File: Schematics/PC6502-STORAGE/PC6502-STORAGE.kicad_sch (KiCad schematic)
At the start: 25 parts, among them J1 BUS, J2 Conn_02x26_Top_Bottom, J3 CLK_SLOW, J99 Conn_02x05_Odd_Even, U1 ATF1502AS

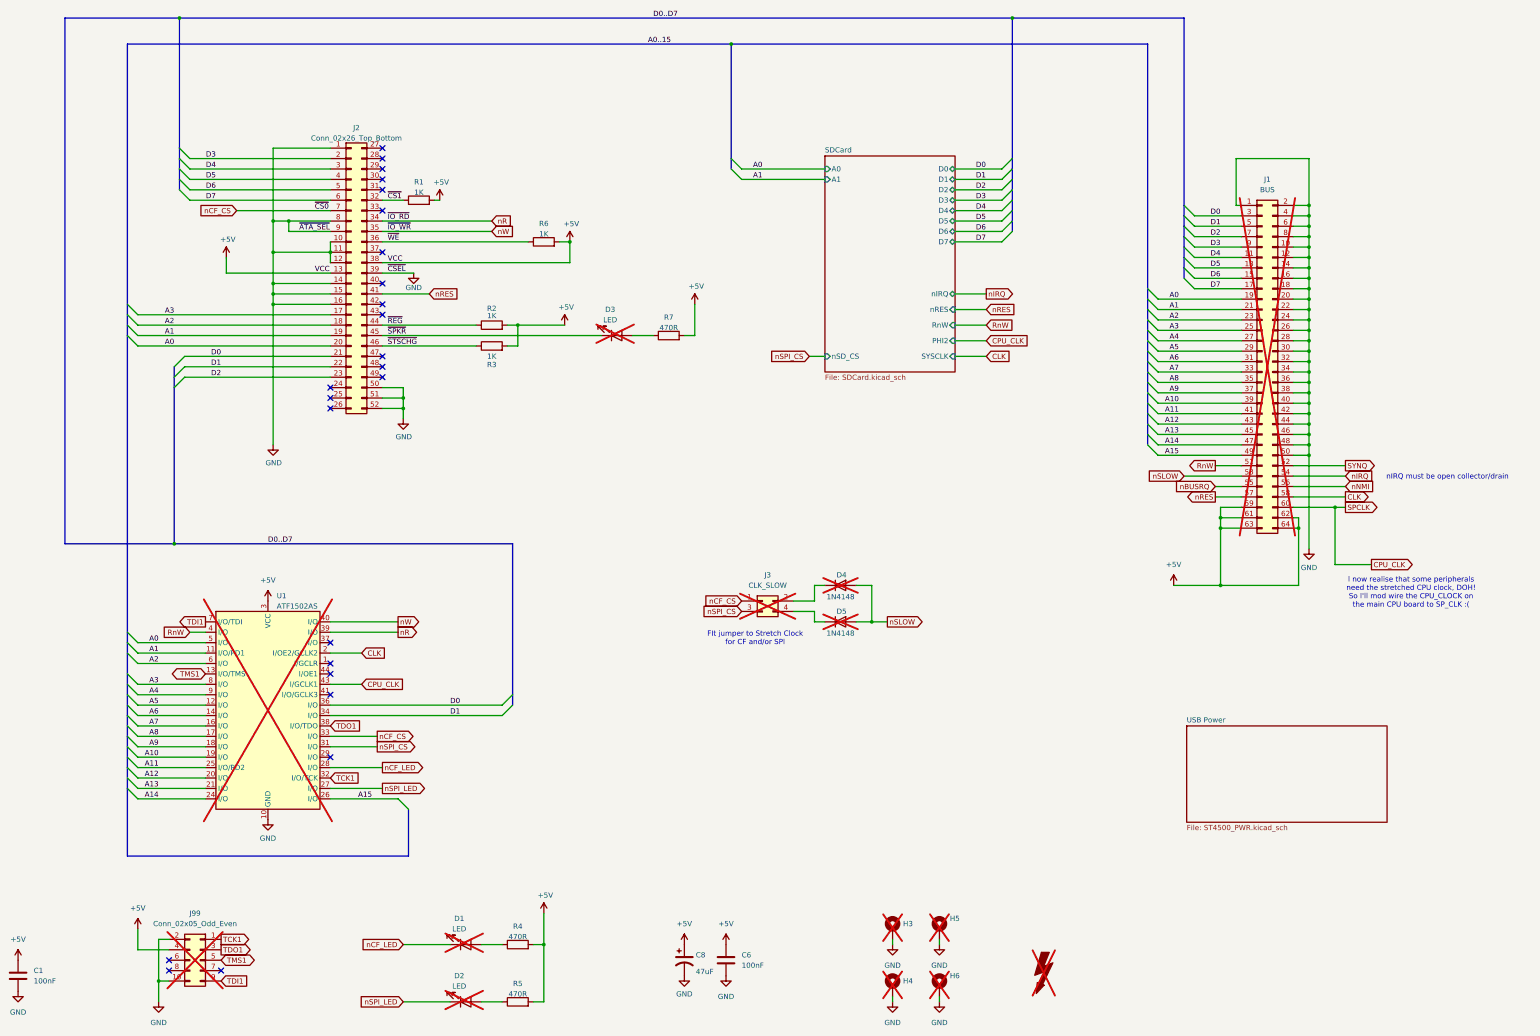
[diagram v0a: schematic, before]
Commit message: Tidy up and simplify
Created schematic for FM & Speech sound board
Made Storage board just for Compact Flash (CF) storage
Routed Storage PCB
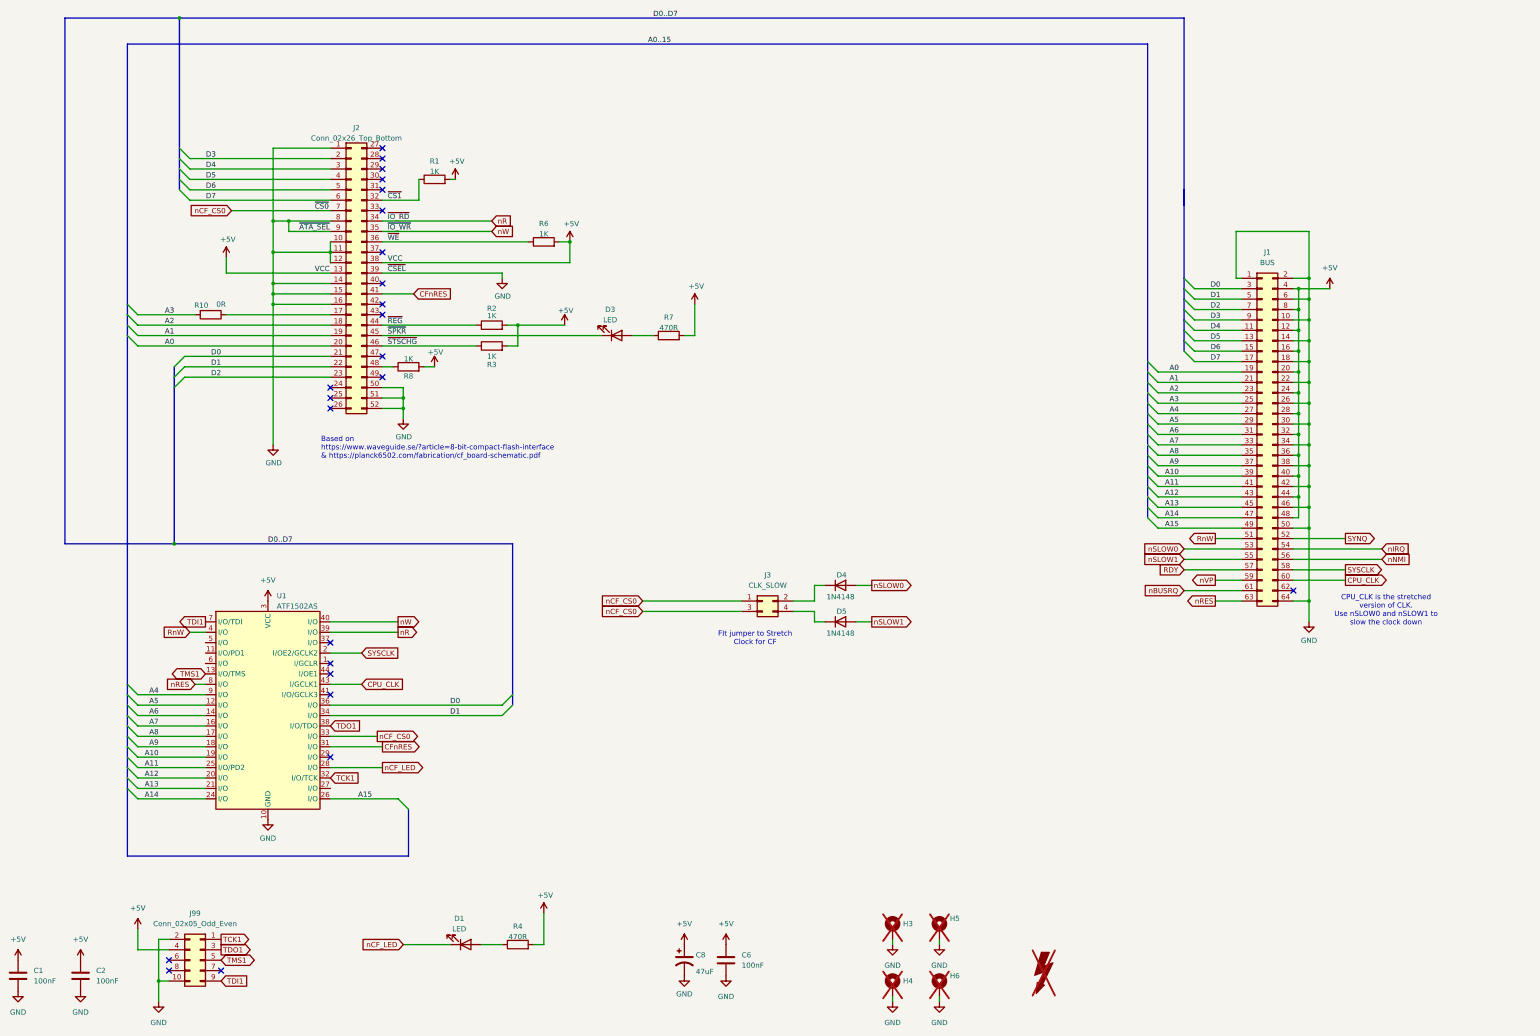
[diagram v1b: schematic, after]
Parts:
- removed D2: LED, LTL-4221NHBP:LTL4221NHBP, symbol Device:LED
- removed R5: 470R, Resistor_SMD:R_0603_1608Metric_Pad0.98x0.95mm_HandSolder, symbol Device:R
- added C2: 100nF, Capacitor_SMD:C_0805_2012Metric, symbol Device:C
- added R10: 0R, Resistor_SMD:R_0603_1608Metric_Pad0.98x0.95mm_HandSolder, symbol Device:R
- added R8: 1K, Resistor_SMD:R_0603_1608Metric_Pad0.98x0.95mm_HandSolder, symbol Device:R
- D1, D3, D4, D5, J1, J3, J99, U1: now fitted
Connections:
- net +5V: now also J1.12 (Pin_12), J1.16 (Pin_16), J1.20 (Pin_20), J1.24 (Pin_24), J1.28 (Pin_28), J1.32 (Pin_32), J1.36 (Pin_36), J1.4 (Pin_4), J1.40 (Pin_40), J1.44 (Pin_44), J1.48 (Pin_48), J1.8 (Pin_8), C2.1, R8.2; no longer J1.59 (Pin_59), J1.61 (Pin_61), J1.62 (Pin_62), J1.63 (Pin_63), J1.64 (Pin_64)
- net A0: no longer U1.5 (I/O)
- net A1: no longer U1.11 (I/O/PD1)
- net A2: no longer U1.6 (I/O)
- net A3: now also R10.2; no longer J2.17 (Pin_17), U1.8 (I/O)
- net GND: now also J1.64 (Pin_64), C2.2; no longer J1.12 (Pin_12), J1.16 (Pin_16), J1.20 (Pin_20), J1.24 (Pin_24), J1.28 (Pin_28), J1.32 (Pin_32), J1.36 (Pin_36), J1.4 (Pin_4), J1.40 (Pin_40), J1.44 (Pin_44), J1.48 (Pin_48), J1.8 (Pin_8)
- net nBUSRQ: now also J1.61 (Pin_61); no longer J1.55 (Pin_55)
- net nRES: now also J1.63 (Pin_63), U1.8 (I/O); no longer J1.57 (Pin_57), J2.41 (Pin_41)
- net at J2.48 (Pin_48): now also R8.1
- net CLK renamed SYSCLK
- net nCF_CS renamed nCF_CS0
- net nCF_CS0: now also J3.3 (Pin_3)
- net nSLOW renamed nSLOW0
- net nSLOW0: no longer D5.2 (A)
- net nSPI_CS renamed CFnRES
- net CFnRES: now also J2.41 (Pin_41); no longer J3.3 (Pin_3)
- net nSPI_LED: no longer names the net of U1.27 (I/O)
- new net: J2.17 (Pin_17), R10.1
- new net RDY: J1.57 (Pin_57)
- new net nSLOW1: D5.2 (A), J1.55 (Pin_55)
- new net nVP: J1.59 (Pin_59)
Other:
- removed sheet SDCard
- removed sheet USB Power
- note added: "Based on https://www.waveguide.se/?article=8-bit-compact-flash-interface & https://planck6502.com/fabrication/cf_board-schematic.pdf"
- note added: "CPU_CLK is the stretched version of CLK. Use nSLOW0 and nSLOW1 to slow the clock down"
- note added: "FIt jumper to Stretch Clock for CF"
- note removed: "FIt jumper to Stretch Clock for CF and/or SPI"
- note removed: "I now realise that some peripherals need the stretched CPU clock, DOH! So I'll mod wire the CPU_CLOCK on the main CPU board to SP_CLK :("
- note removed: "nIRQ must be open collector/drain"
- moved on the sheet: R1
